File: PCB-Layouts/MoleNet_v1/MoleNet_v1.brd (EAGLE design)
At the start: 82.9 x 70.2 mm, 26 parts, among them IC1 25LC080P, K1 ISP, Q1 BS250, Q2 BS170, U1 MCP1703-5002E/DB, U3 RFM69CW, U4 ATMEGA328P-PU, X1 SMA-142-0701-851/861

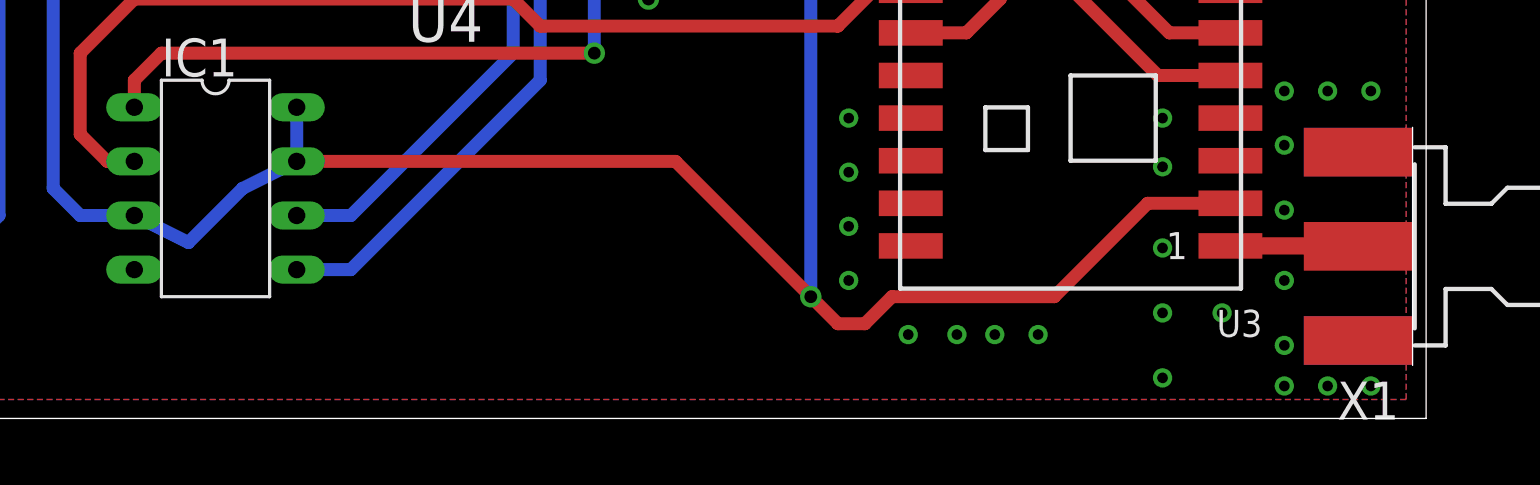
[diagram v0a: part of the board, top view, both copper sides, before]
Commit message: corrected SMA connector of MoleNet v1
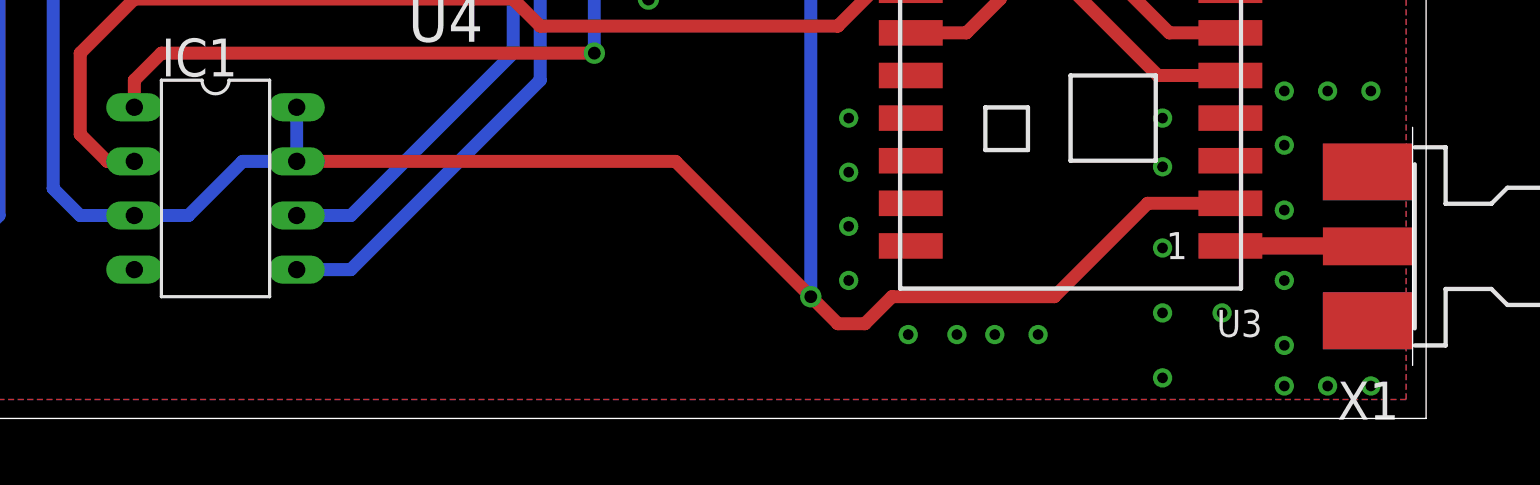
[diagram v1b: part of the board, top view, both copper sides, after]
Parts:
- X1: value SMA-142-0701-851/861 -> SMA-142-0711-821/826; device con-coax:J502-ND-142-0701-851/861 -> con-coax:J502-ND-142-0711-821/826
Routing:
- net VCC: track 264.3 -> 263.7 mm
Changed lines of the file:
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@@
 </element>
 <element name="U3" library="SparkFun-RF" package="RFM69CW-XXXS2" value="RFM69CW" x="65.8495" y="13.462" rot="R180"/>
-<element name="X1" library="con-coax" package="J502-ND-142-0701-851/861" value="SMA-142-0701-851/861" x="81.9023" y="7.4422" rot="R180">
-<attribute name="OC_NEWARK" value="99F6798" x="81.9023" y="7.4422" size="1.778" layer="27" rot="R180" display="off"/>
-<attribute name="MPN" value="142-0701-851" x="81.9023" y="7.4422" size="1.778" layer="27" rot="R180" display="off"/>
+<element name="X1" library="con-coax" package="J502-ND-142-0711-821/826" value="SMA-142-0711-821/826" x="81.9023" y="7.4422" rot="R180">
+<attribute name="OC_NEWARK" value="16F3627" x="81.9023" y="7.4422" size="1.778" layer="27" rot="R180" display="off"/>
+<attribute name="MPN" value="142-0711-821" x="81.9023" y="7.4422" size="1.778" layer="27" rot="R180" display="off"/>
 <attribute name="MF" value="JOHNSON COMPONENTS" x="81.9023" y="7.4422" size="1.778" layer="27" rot="R180" display="off"/>
-<attribute name="OC_FARNELL" value="1019325" x="81.9023" y="7.4422" size="1.778" layer="27" rot="R180" display="off"/>
+<attribute name="OC_FARNELL" value="1019328" x="81.9023" y="7.4422" size="1.778" layer="27" rot="R180" display="off"/>
 </element>
 <element name="C5" library="resistor" package="C025-025X050" value="" x="32.0675" y="41.91" rot="R90"/>
@@
 <contactref element="U3" pad="1"/>
 <wire x1="80.1949" y1="7.462" x2="79.76388125" y2="7.453334375" width="0.6096" layer="1"/>
-<wire x1="79.76388125" y1="7.453334375" x2="79.3369" y2="7.4422" width="0.6096" layer="1"/>
+<wire x1="79.76388125" y1="7.453334375" x2="79.7869" y2="7.4422" width="0.6096" layer="1"/>
 <wire x1="73.3495" y1="7.462" x2="80.1949" y2="7.462" width="0.8128" layer="1"/>
 </signal>
@@
 <wire x1="53.6575" y1="25.4" x2="54.9275" y2="26.67" width="0.6096" layer="16"/>
 <wire x1="53.6575" y1="5.08" x2="53.6575" y2="25.4" width="0.6096" layer="16"/>
-<wire x1="21.9075" y1="8.89" x2="24.4475" y2="7.62" width="0.6096" layer="16"/>
-<wire x1="24.4475" y1="7.62" x2="26.9875" y2="10.16" width="0.6096" layer="16"/>
-<wire x1="26.9875" y1="10.16" x2="29.5275" y2="11.43" width="0.6096" layer="16"/>
+<wire x1="21.9075" y1="8.89" x2="24.4475" y2="8.89" width="0.6096" layer="16"/>
+<wire x1="24.4475" y1="8.89" x2="26.9875" y2="11.43" width="0.6096" layer="16"/>
+<wire x1="26.9875" y1="11.43" x2="29.5275" y2="11.43" width="0.6096" layer="16"/>
 <wire x1="18.0975" y1="10.16" x2="19.3675" y2="8.89" width="0.6096" layer="16"/>
 <wire x1="19.3675" y1="8.89" x2="21.9075" y2="8.89" width="0.6096" layer="16"/>

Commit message: added/corrected part values in all layouts; created partlist for version 2.1
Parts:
- C1: value 10uF -> 4.7uF
- C2, C3: value (none) -> 1uF
- C4, C5, C6, C9: value (none) -> 100nF
- C7, C8: value (none) -> 22pF
- L1: value (none) -> 10mH
- Q3: value (none) -> 8MHz
- R1: value (none) -> 10k
- R2: value (none) -> 100k
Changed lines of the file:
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@@
 <element name="Q2" library="transistor-small-signal" package="SOT54E" value="BS170" x="11.7475" y="38.1" rot="R270"/>
 <element name="Q1" library="transistor-small-signal" package="SOT54E" value="BS250" x="6.6675" y="38.1" rot="R90"/>
-<element name="R2" library="resistor" package="0207/10" value="" x="2.8575" y="45.72" rot="R90"/>
+<element name="R2" library="resistor" package="0207/10" value="100k" x="2.8575" y="45.72" rot="R90"/>
 <element name="RTC" library="con-phoenix-254" package="7POL254" value="" x="66.3575" y="54.61" smashed="yes" rot="R180">
 <attribute name="OC_NEWARK" value="unknown" x="66.3575" y="54.61" size="1.778" layer="27" rot="R180" display="off"/>
@@
 <attribute name="VALUE" x="75.5015" y="57.658" size="1.27" layer="27" rot="R180"/>
 </element>
-<element name="L1" library="inductor-neosid" package="BS11" value="" x="52.4256" y="27.305" rot="R180">
+<element name="L1" library="inductor-neosid" package="BS11" value="10mH" x="52.4256" y="27.305" rot="R180">
 <attribute name="OC_FARNELL" value="unknown" x="52.4256" y="27.305" size="1.778" layer="27" rot="R180" display="off"/>
 <attribute name="MF" value="" x="52.4256" y="27.305" size="1.778" layer="27" rot="R180" display="off"/>
@@
 <attribute name="MPN" value="" x="52.4256" y="27.305" size="1.778" layer="27" rot="R180" display="off"/>
 </element>
-<element name="C1" library="resistor" package="E2,5-6" value="10uF" x="4.1275" y="55.88" rot="R180"/>
-<element name="C2" library="resistor" package="C025-025X050" value="" x="9.2075" y="52.07" rot="R90"/>
-<element name="C3" library="resistor" package="C025-025X050" value="" x="23.1775" y="52.07" rot="R90"/>
-<element name="C4" library="resistor" package="C025-025X050" value="" x="51.1175" y="35.56" smashed="yes">
+<element name="C1" library="resistor" package="E2,5-6" value="4.7uF" x="4.1275" y="55.88" rot="R180"/>
+<element name="C2" library="resistor" package="C025-025X050" value="1uF" x="9.2075" y="52.07" rot="R90"/>
+<element name="C3" library="resistor" package="C025-025X050" value="1uF" x="23.1775" y="52.07" rot="R90"/>
+<element name="C4" library="resistor" package="C025-025X050" value="100nF" x="51.1175" y="35.56" smashed="yes">
 <attribute name="NAME" x="53.9115" y="34.544" size="1.27" layer="25" ratio="10"/>
 <attribute name="VALUE" x="48.8315" y="32.766" size="1.27" layer="27" ratio="10"/>
 </element>
-<element name="C6" library="resistor" package="C025-025X050" value="" x="51.1175" y="38.100003125" smashed="yes">
+<element name="C6" library="resistor" package="C025-025X050" value="100nF" x="51.1175" y="38.100003125" smashed="yes">
 <attribute name="NAME" x="53.9115" y="38.354003125" size="1.27" layer="25" ratio="10"/>
 <attribute name="VALUE" x="48.8315" y="35.306003125" size="1.27" layer="27" ratio="10"/>
@@
 <attribute name="OC_FARNELL" value="1019328" x="81.9023" y="7.4422" size="1.778" layer="27" rot="R180" display="off"/>
 </element>
-<element name="C5" library="resistor" package="C025-025X050" value="" x="32.0675" y="41.91" rot="R90"/>
+<element name="C5" library="resistor" package="C025-025X050" value="100nF" x="32.0675" y="41.91" rot="R90"/>
 <element name="JP2" library="pinhead" package="1X06" value="" x="19.3675" y="63.5" rot="R180"/>
-<element name="C9" library="resistor" package="C025-025X050" value="" x="29.5275" y="62.23" rot="R90"/>
-<element name="R1" library="resistor" package="0207/10" value="" x="23.1775" y="58.42" rot="R180"/>
-<element name="Q3" library="crystal" package="HC18U-V" value="" x="28.2575" y="33.02" rot="R270">
+<element name="C9" library="resistor" package="C025-025X050" value="100nF" x="29.5275" y="62.23" rot="R90"/>
+<element name="R1" library="resistor" package="0207/10" value="10k" x="23.1775" y="58.42" rot="R180"/>
+<element name="Q3" library="crystal" package="HC18U-V" value="8MHz" x="28.2575" y="33.02" rot="R270">
 <attribute name="OC_FARNELL" value="unknown" x="28.2575" y="33.02" size="1.778" layer="27" rot="R270" display="off"/>
 <attribute name="MF" value="" x="28.2575" y="33.02" size="1.778" layer="27" rot="R270" display="off"/>
@@
 <attribute name="MPN" value="" x="28.2575" y="33.02" size="1.778" layer="27" rot="R270" display="off"/>
 </element>
-<element name="C7" library="resistor" package="C025-025X050" value="" x="21.9075" y="35.56" rot="R180"/>
-<element name="C8" library="resistor" package="C025-025X050" value="" x="21.9075" y="30.48" rot="R180"/>
+<element name="C7" library="resistor" package="C025-025X050" value="22pF" x="21.9075" y="35.56" rot="R180"/>
+<element name="C8" library="resistor" package="C025-025X050" value="22pF" x="21.9075" y="30.48" rot="R180"/>
 <element name="U4" library="Atmel_By_element14_Batch_1-00" package="DIP254P762X457-28" value="ATMEGA328P-PU" x="43.4975" y="22.86">
 <attribute name="OC_FARNELL" value="1715487" x="43.4975" y="22.86" size="1.778" layer="27" display="off"/>
